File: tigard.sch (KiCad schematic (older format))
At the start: 90 parts, among them J1 USB_C_Receptacle_USB2.0, J2 JTAG, J3 UART, J4 SPI, J5 CORTEX, J6 LA, J7 I2C, Q1 BSH103, SW1 TARGET, SW2 MODE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

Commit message: Add CDONE pin for iCE programming (#15)
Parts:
- added R22: 2k2, Resistor_SMD:R_0402_1005Metric, symbol Device:R_Small
- J2: footprint tigard:PinHeader_1x08_P2.54mm_Vertical -> tigard:PinHeader_1x09_P2.54mm_Vertical; symbol Connector_Generic:Conn_01x08 -> Connector_Generic:Conn_01x09
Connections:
- net UART_RX is gone; now on net ICE_CDONE: J3.4 (Pin_4), J6.8 (Pin_8), RN7.1 (R1.1), U6.21 (B1)
- net BD5: now also R22.1
- net BD6: now reaches RN6.2 (R2.1)
- net BD6: now also U3.45 (BDBUS6)
- net ICE_CDONE: now reaches RN8.2 (R2.1), U6.16 (B6)
- net ICE_CDONE: now also J2.9 (Pin_9)
- net BD7: now reaches U3.46 (BDBUS7)
- net BD7: now also R22.2
- no-connect marks 34 -> 31
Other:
- note added: "Populate with 8 pin header"
- note added: "iCE40 Programming"
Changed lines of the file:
@@
 Wire Wire Line
 	10800 2500 10800 2550
-$Comp
-L Connector_Generic:Conn_01x09 J3
-U 1 1 5EBEAC72
-P 11600 1250
-F 0 "J3" H 11680 1292 50  0000 L CNN
-F 1 "UART" H 11680 1201 50  0000 L CNN
-F 2 "tigard:PinHeader_1x09_P2.54mm_Vertical" H 11600 1250 50  0001 C CNN
-F 3 "~" H 11600 1250 50  0001 C CNN
-F 4 "MTP125-1108S1" H 11600 1250 50  0001 C CNN "P/N"
-F 5 "C358689" H 11600 1250 50  0001 C CNN "LCSC"
-F 6 "conn-th-01in-9-1-hdr" H 11600 1250 50  0001 C CNN "Key"
-	1    11600 1250
-	1    0    0    -1
-$EndComp
-Text Label 11000 1050 0    50   ~ 0
-UART_TX
-Text Label 11000 1150 0    50   ~ 0
-UART_RX
-Text Label 11000 1250 0    50   ~ 0
-~UART_RTS
-Text Label 11000 1350 0    50   ~ 0
-~UART_CTS
-Text Label 11000 1450 0    50   ~ 0
-~UART_DTR
-Text Label 11000 1550 0    50   ~ 0
-~UART_DSR
-Text Label 11000 1650 0    50   ~ 0
-~UART_DCD
-$Comp
-L power:GND #PWR0122
-U 1 1 5ECE873D
-P 10800 950
-F 0 "#PWR0122" H 10800 700 50  0001 C CNN
-F 1 "GND" H 10805 777 50  0000 C CNN
-F 2 "" H 10800 950 50  0001 C CNN
-F 3 "" H 10800 950 50  0001 C CNN
-	1    10800 950
-	1    0    0    -1
-$EndComp
-Wire Wire Line
-	10800 950  11400 950
-Wire Wire Line
-	11400 1050 11000 1050
-Wire Wire Line
-	11000 1150 11400 1150
-Wire Wire Line
-	11000 1250 11400 1250
-Wire Wire Line
-	11400 1350 11000 1350
-Wire Wire Line
-	11000 1450 11400 1450
-Wire Wire Line
-	11000 1550 11400 1550
-Wire Wire Line
-	11400 1650 11000 1650
 Text Notes 11050 4550 0    100  Italic 20
 CONNECTORS
@@
 Wire Wire Line
 	4150 6750 3900 6750
-Wire Wire Line
-	3900 6850 4150 6850
 NoConn ~ 3900 5250
 NoConn ~ 3900 5450
@@
 NoConn ~ 3900 6050
 NoConn ~ 3900 6150
-NoConn ~ 3900 6950
-NoConn ~ 3900 7050
 NoConn ~ 3900 7250
 NoConn ~ 3900 7350
@@
 L power:GND #PWR0121
 U 1 1 5F53C62A
-P 9350 1000
-F 0 "#PWR0121" H 9350 750 50  0001 C CNN
-F 1 "GND" H 9355 827 50  0000 C CNN
-F 2 "" H 9350 1000 50  0001 C CNN
-F 3 "" H 9350 1000 50  0001 C CNN
-	1    9350 1000
-	1    0    0    -1
-$EndComp
-Wire Wire Line
-	9350 1000 9900 1000
-Wire Wire Line
-	9900 1600 9550 1600
-Wire Wire Line
-	9550 1300 9900 1300
-Wire Wire Line
-	9900 1100 9550 1100
-Wire Wire Line
-	9550 1400 9900 1400
-Wire Wire Line
-	9900 1200 9550 1200
-Wire Wire Line
-	9550 1500 9900 1500
-Text Label 9550 1600 0    50   ~ 0
+P 9200 900
+F 0 "#PWR0121" H 9200 650 50  0001 C CNN
+F 1 "GND" H 9205 727 50  0000 C CNN
+F 2 "" H 9200 900 50  0001 C CNN
+F 3 "" H 9200 900 50  0001 C CNN
+	1    9200 900
+	1    0    0    -1
+$EndComp
+Text Label 9400 1500 0    50   ~ 0
 ~SRST
-Text Label 9550 1300 0    50   ~ 0
+Text Label 9400 1200 0    50   ~ 0
 TDO
-Text Label 9550 1100 0    50   ~ 0
+Text Label 9400 1000 0    50   ~ 0
 TCK
-Text Label 9550 1400 0    50   ~ 0
+Text Label 9400 1300 0    50   ~ 0
 TMS
-Text Label 9550 1200 0    50   ~ 0
+Text Label 9400 1100 0    50   ~ 0
 TDI
-Text Label 9550 1500 0    50   ~ 0
+Text Label 9400 1400 0    50   ~ 0
 ~TRST
-$Comp
-L Connector_Generic:Conn_01x08 J2
-U 1 1 5F7118A4
-P 10100 1200
-F 0 "J2" H 10180 1192 50  0000 L CNN
-F 1 "JTAG" H 10180 1101 50  0000 L CNN
-F 2 "tigard:PinHeader_1x08_P2.54mm_Vertical" H 10100 1200 50  0001 C CNN
-F 3 "~" H 10100 1200 50  0001 C CNN
-F 4 "MTP125-1108S1" H 10100 1200 50  0001 C CNN "P/N"
-F 5 "C358689" H 10100 1200 50  0001 C CNN "LCSC"
-F 6 "conn-th-01in-8-1-hdr" H 10100 1200 50  0001 C CNN "Key"
-	1    10100 1200
-	1    0    0    -1
-$EndComp
 $Comp
 L Device:C_Small C7
@@
 Text Label 5400 7400 0    50   ~ 0
 AD1
-NoConn ~ 5600 7900
 NoConn ~ 5600 8000
 NoConn ~ 5600 8100
 Wire Wire Line
 	5600 8000 5650 8000
-Wire Wire Line
-	5600 7900 5650 7900
 Wire Wire Line
 	5650 8100 5600 8100
@@
 L tigard:VTARGET #PWR0141
 U 1 1 5FBCFE64
-P 9800 850
-F 0 "#PWR0141" H 9800 700 50  0001 C CNN
-F 1 "VTARGET" H 9815 1023 50  0000 C CNN
-F 2 "" H 9800 850 50  0001 C CNN
-F 3 "" H 9800 850 50  0001 C CNN
-	1    9800 850
-	1    0    0    -1
-$EndComp
-Wire Wire Line
-	9800 850  9800 900
-Wire Wire Line
-	9800 900  9900 900
-$Comp
-L tigard:VTARGET #PWR0148
-U 1 1 5FC9CE0F
-P 11300 800
-F 0 "#PWR0148" H 11300 650 50  0001 C CNN
-F 1 "VTARGET" H 11315 973 50  0000 C CNN
-F 2 "" H 11300 800 50  0001 C CNN
-F 3 "" H 11300 800 50  0001 C CNN
-	1    11300 800
-	1    0    0    -1
-$EndComp
-Wire Wire Line
-	11300 800  11300 850
-Wire Wire Line
-	11300 850  11400 850
+P 9800 750
+F 0 "#PWR0141" H 9800 600 50  0001 C CNN
+F 1 "VTARGET" H 9815 923 50  0000 C CNN
+F 2 "" H 9800 750 50  0001 C CNN
+F 3 "" H 9800 750 50  0001 C CNN
+	1    9800 750
+	1    0    0    -1
+$EndComp
+Wire Wire Line
+	9800 750  9800 800
+Wire Wire Line
+	9800 800  9900 800
 $Comp
 L tigard:VTARGET #PWR0149
@@
 Connection ~ 3300 2700
 $Comp
-L power:GND #PWR?
+L power:GND #PWR04
 U 1 1 5F303A88
 P 10150 3800
-F 0 "#PWR?" H 10150 3550 50  0001 C CNN
+F 0 "#PWR04" H 10150 3550 50  0001 C CNN
 F 1 "GND" H 10155 3627 50  0000 C CNN
 F 2 "" H 10150 3800 50  0001 C CNN
@@
 Wire Wire Line
 	10150 3750 10150 3800
+Text Label 4150 6950 2    50   ~ 0
+BD6
+Text Label 4150 7050 2    50   ~ 0
+BD7
+Wire Wire Line
+	3900 6950 4150 6950
+$Comp
+L Device:R_Small R22
+U 1 1 5F59250B
+P 4350 6950
+F 0 "R22" H 4409 6996 50  0000 L CNN
+F 1 "2k2" H 4409 6905 50  0000 L CNN
+F 2 "Resistor_SMD:R_0402_1005Metric" H 4350 6950 50  0001 C CNN
+F 3 "~" H 4350 6950 50  0001 C CNN
+F 4 "0402WGJ0222TCE" H 4350 6950 50  0001 C CNN "P/N"
+F 5 "C25933" H 4350 6950 50  0001 C CNN "LCSC"
+F 6 "res-0402-2k2" H 4350 6950 50  0001 C CNN "Key"
+	1    4350 6950
+	1    0    0    -1
+$EndComp
+Wire Wire Line
+	3900 7050 4350 7050
+Wire Wire Line
+	3900 6850 4350 6850
+Text Label 5400 7900 0    50   ~ 0
+BD6
+Wire Wire Line
+	5400 7900 5650 7900
+Text Label 7350 8600 0    50   ~ 0
+UART_RX
+Text Notes 7400 8750 0    50   ~ 0
+iCE40 Programming
+Text Label 8050 7900 2    50   ~ 0
+ICE_CDONE
+Text Label 8250 8600 2    50   ~ 0
+ICE_CDONE
+Wire Wire Line
+	7350 8600 8250 8600
+Wire Wire Line
+	11300 850  11400 850
+Wire Wire Line
+	11300 800  11300 850
+$Comp
+L tigard:VTARGET #PWR0148
+U 1 1 5FC9CE0F
+P 11300 800
+F 0 "#PWR0148" H 11300 650 50  0001 C CNN
+F 1 "VTARGET" H 11315 973 50  0000 C CNN
+F 2 "" H 11300 800 50  0001 C CNN
+F 3 "" H 11300 800 50  0001 C CNN
+	1    11300 800
+	1    0    0    -1
+$EndComp
+Wire Wire Line
+	11400 1650 11000 1650
+Wire Wire Line
+	11000 1550 11400 1550
+Wire Wire Line
+	11000 1450 11400 1450
+Wire Wire Line
+	11400 1350 11000 1350
+Wire Wire Line
+	11000 1250 11400 1250
+Wire Wire Line
+	11000 1150 11400 1150
+Wire Wire Line
+	11400 1050 11000 1050
+Wire Wire Line
+	10800 950  11400 950
+$Comp
+L power:GND #PWR0122
+U 1 1 5ECE873D
+P 10800 950
+F 0 "#PWR0122" H 10800 700 50  0001 C CNN
+F 1 "GND" H 10805 777 50  0000 C CNN
+F 2 "" H 10800 950 50  0001 C CNN
+F 3 "" H 10800 950 50  0001 C CNN
+	1    10800 950
+	1    0    0    -1
+$EndComp
+Text Label 11000 1650 0    50   ~ 0
+~UART_DCD
+Text Label 11000 1550 0    50   ~ 0
+~UART_DSR
+Text Label 11000 1450 0    50   ~ 0
+~UART_DTR
+Text Label 11000 1350 0    50   ~ 0
+~UART_CTS
+Text Label 11000 1250 0    50   ~ 0
+~UART_RTS
+Text Label 11000 1150 0    50   ~ 0
+UART_RX
+Text Label 11000 1050 0    50   ~ 0
+UART_TX
+$Comp
+L Connector_Generic:Conn_01x09 J3
+U 1 1 5EBEAC72
+P 11600 1250
+F 0 "J3" H 11680 1292 50  0000 L CNN
+F 1 "UART" H 11680 1201 50  0000 L CNN
+F 2 "tigard:PinHeader_1x09_P2.54mm_Vertical" H 11600 1250 50  0001 C CNN
+F 3 "~" H 11600 1250 50  0001 C CNN
+F 4 "MTP125-1108S1" H 11600 1250 50  0001 C CNN "P/N"
+F 5 "C358689" H 11600 1250 50  0001 C CNN "LCSC"
+F 6 "conn-th-01in-9-1-hdr" H 11600 1250 50  0001 C CNN "Key"
+	1    11600 1250
+	1    0    0    -1
+$EndComp
+$Comp
+L Connector_Generic:Conn_01x09 J2
+U 1 1 5F7118A4
+P 10100 1200
+F 0 "J2" H 10180 1192 50  0000 L CNN
+F 1 "JTAG" H 10180 1101 50  0000 L CNN
+F 2 "tigard:PinHeader_1x09_P2.54mm_Vertical" H 10100 1200 50  0001 C CNN
+F 3 "~" H 10100 1200 50  0001 C CNN
+F 4 "MTP125-1108S1" H 10100 1200 50  0001 C CNN "P/N"
+F 5 "C358689" H 10100 1200 50  0001 C CNN "LCSC"
+F 6 "conn-th-01in-8-1-hdr" H 10100 1200 50  0001 C CNN "Key"
+	1    10100 1200
+	1    0    0    -1
+$EndComp
+Text Notes 9650 1750 0    50   ~ 0
+Populate with 8 pin header
+Text Label 9400 1600 0    50   ~ 0
+ICE_CDONE
+Wire Wire Line
+	9400 1500 9900 1500
+Wire Wire Line
+	9400 1400 9900 1400
+Wire Wire Line
+	9400 1300 9900 1300
+Wire Wire Line
+	9400 1200 9900 1200
+Wire Wire Line
+	9400 1100 9900 1100
+Wire Wire Line
+	9400 1000 9900 1000
+Wire Wire Line
+	9200 900  9900 900
+Wire Wire Line
+	9400 1600 9900 1600
 $EndSCHEMATC

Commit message: fixing 1.27mm header part numbers
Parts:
- J5: LCSC C239059 -> C448647; P/N 20021111-00010T4LF -> FTSH-105-01-F-DV-K
- J6: LCSC (none) -> C448647; P/N (none) -> FTSH-107-01-F-DV-K
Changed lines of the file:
@@
 F 2 "tigard:PinHeader_2x05_P1.27mm_Vertical_SMD" H 11150 2300 50  0001 C CNN
 F 3 "~" H 11150 2300 50  0001 C CNN
-F 4 "20021111-00010T4LF" H 11150 2300 50  0001 C CNN "P/N"
-F 5 "C239059" H 11150 2300 50  0001 C CNN "LCSC"
+F 4 "FTSH-105-01-F-DV-K" H 11150 2300 50  0001 C CNN "P/N"
+F 5 "C448647" H 11150 2300 50  0001 C CNN "LCSC"
 F 6 "conn-th-01in-5-2-hdr" H 11150 2300 50  0001 C CNN "Key"
 	1    11150 2300
@@
 F 2 "tigard:PinHeader_2x07_P1.27mm_Vertical_SMD" H 9750 3350 50  0001 C CNN
 F 3 "~" H 9750 3350 50  0001 C CNN
+F 4 "FTSH-107-01-F-DV-K" H 9750 3350 50  0001 C CNN "P/N"
+F 5 "C448647" H 9750 3350 50  0001 C CNN "LCSC"
 	1    9750 3350
 	1    0    0    -1

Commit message: fixing uart header component; JTAG header label
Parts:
- J3: LCSC C358689 -> C492408; P/N MTP125-1108S1 -> PZ254V-11-09P
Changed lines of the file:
@@
 F 2 "tigard:PinHeader_1x09_P2.54mm_Vertical" H 11600 1250 50  0001 C CNN
 F 3 "~" H 11600 1250 50  0001 C CNN
-F 4 "MTP125-1108S1" H 11600 1250 50  0001 C CNN "P/N"
-F 5 "C358689" H 11600 1250 50  0001 C CNN "LCSC"
+F 4 "PZ254V-11-09P" H 11600 1250 50  0001 C CNN "P/N"
+F 5 "C492408" H 11600 1250 50  0001 C CNN "LCSC"
 F 6 "conn-th-01in-9-1-hdr" H 11600 1250 50  0001 C CNN "Key"
 	1    11600 1250

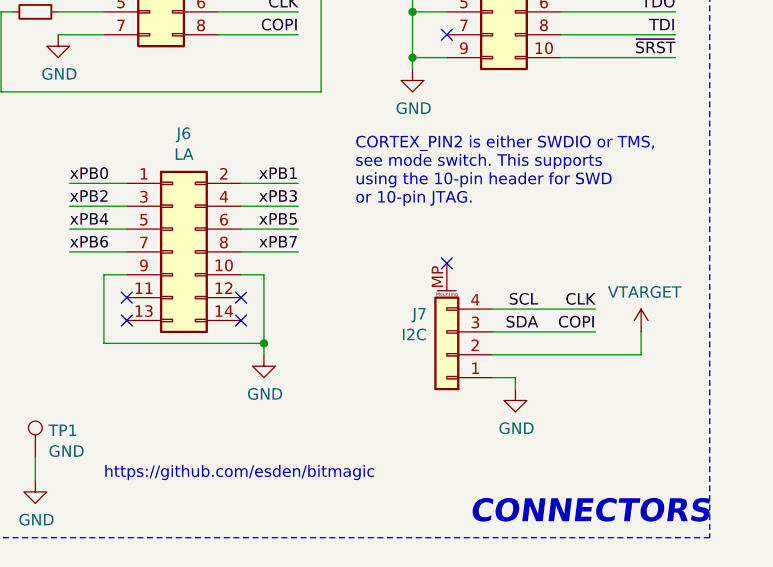
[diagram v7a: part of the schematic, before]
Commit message: Move LA and qwiic over (closes #28)
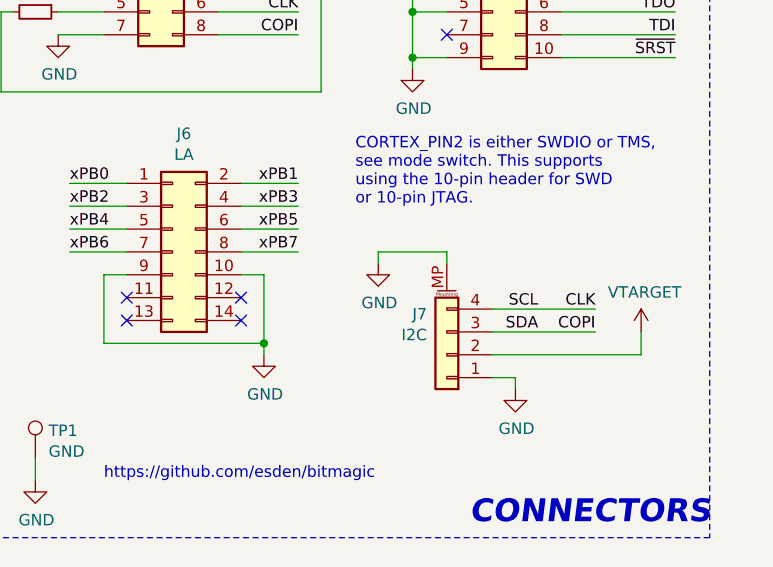
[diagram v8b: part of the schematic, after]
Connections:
- net GND: now also J7.MP (MountPin)
- no-connect marks 31 -> 30
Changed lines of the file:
@@
 Text Label 11350 3600 2    50   ~ 0
 SCL
-NoConn ~ 10950 3400
 Wire Notes Line
 	8800 4050 4800 4050
@@
 Wire Wire Line
 	9400 1600 9900 1600
+$Comp
+L power:GND #PWR?
+U 1 1 5FA57912
+P 10650 3400
+F 0 "#PWR?" H 10650 3150 50  0001 C CNN
+F 1 "GND" H 10655 3227 50  0000 C CNN
+F 2 "" H 10650 3400 50  0001 C CNN
+F 3 "" H 10650 3400 50  0001 C CNN
+	1    10650 3400
+	1    0    0    -1
+$EndComp
+Wire Wire Line
+	10650 3400 10650 3350
+Wire Wire Line
+	10650 3350 10950 3350
+Wire Wire Line
+	10950 3350 10950 3400
 $EndSCHEMATC
